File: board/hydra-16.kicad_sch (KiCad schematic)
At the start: 35 parts, among them J1 Conn_01x32, J2 Conn_01x24, J3 DSUB_9, J4 RDY Pull_Up, U1 WDC65C02S, U2 R65C22-P2, U3 R65C51-P2, U4 74F138, U5 MAX232, U6 SST39SF0x0A, U7 HM628512LP-5

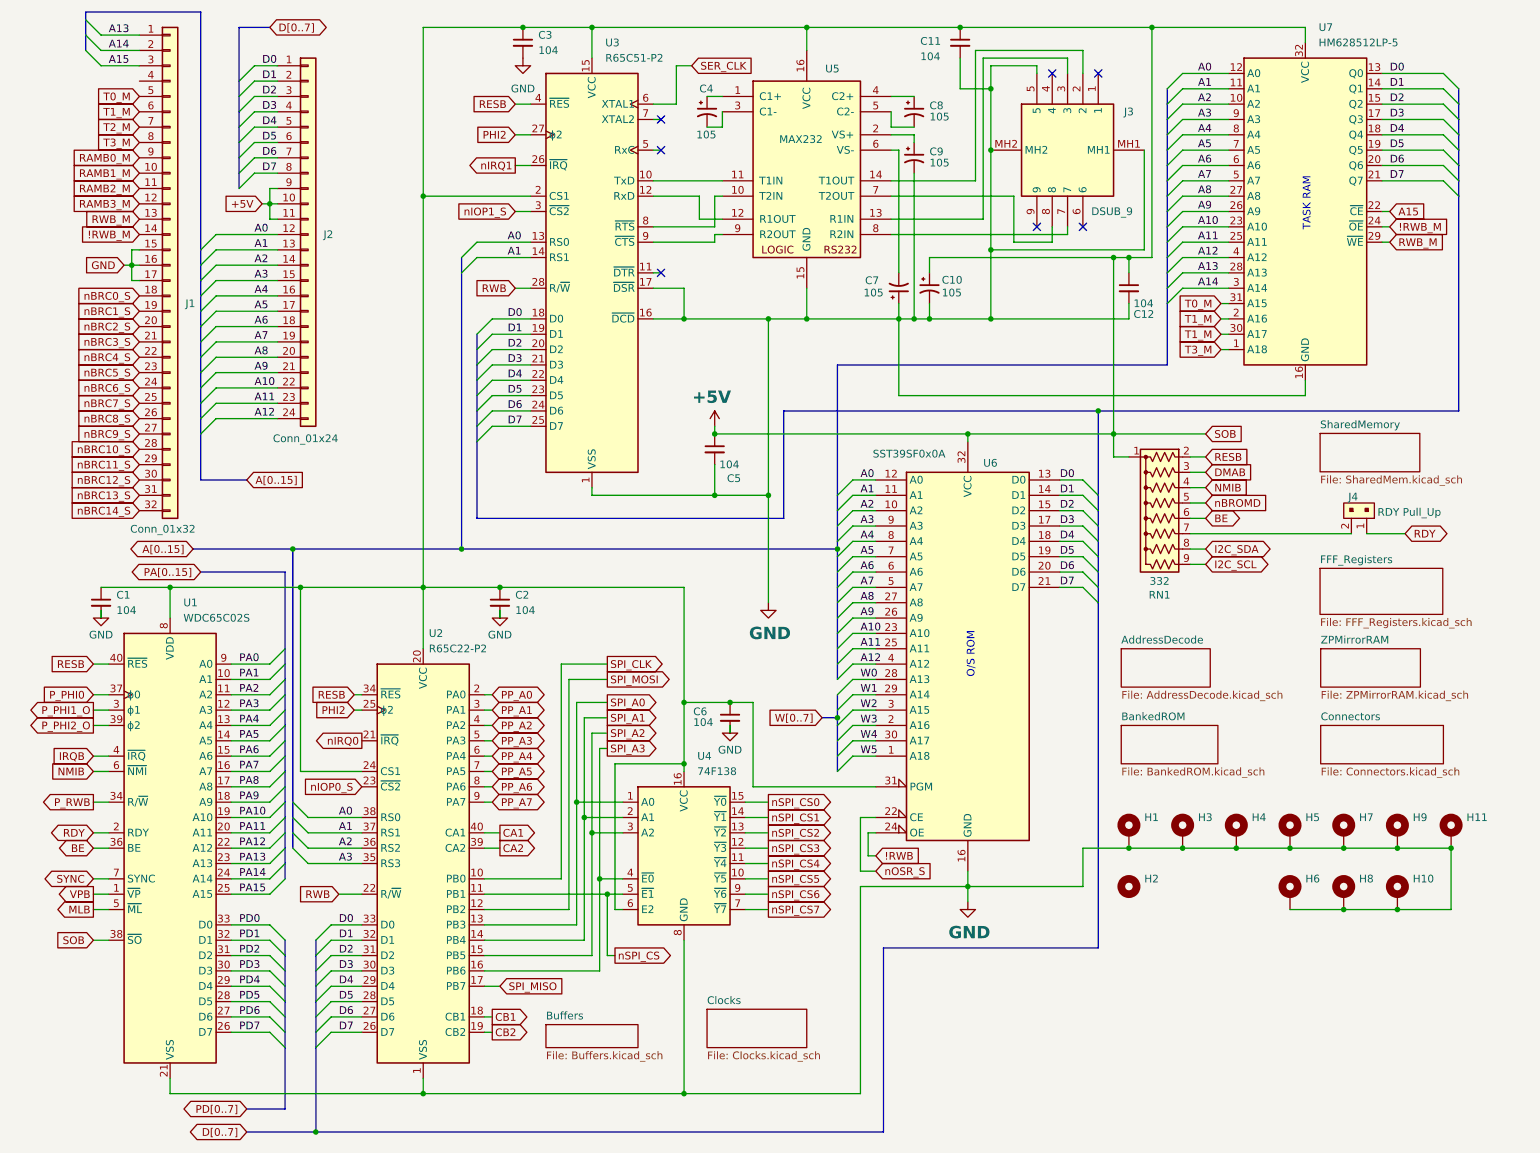
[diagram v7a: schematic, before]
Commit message: 1.7C: Logic corrections and placement tweaks
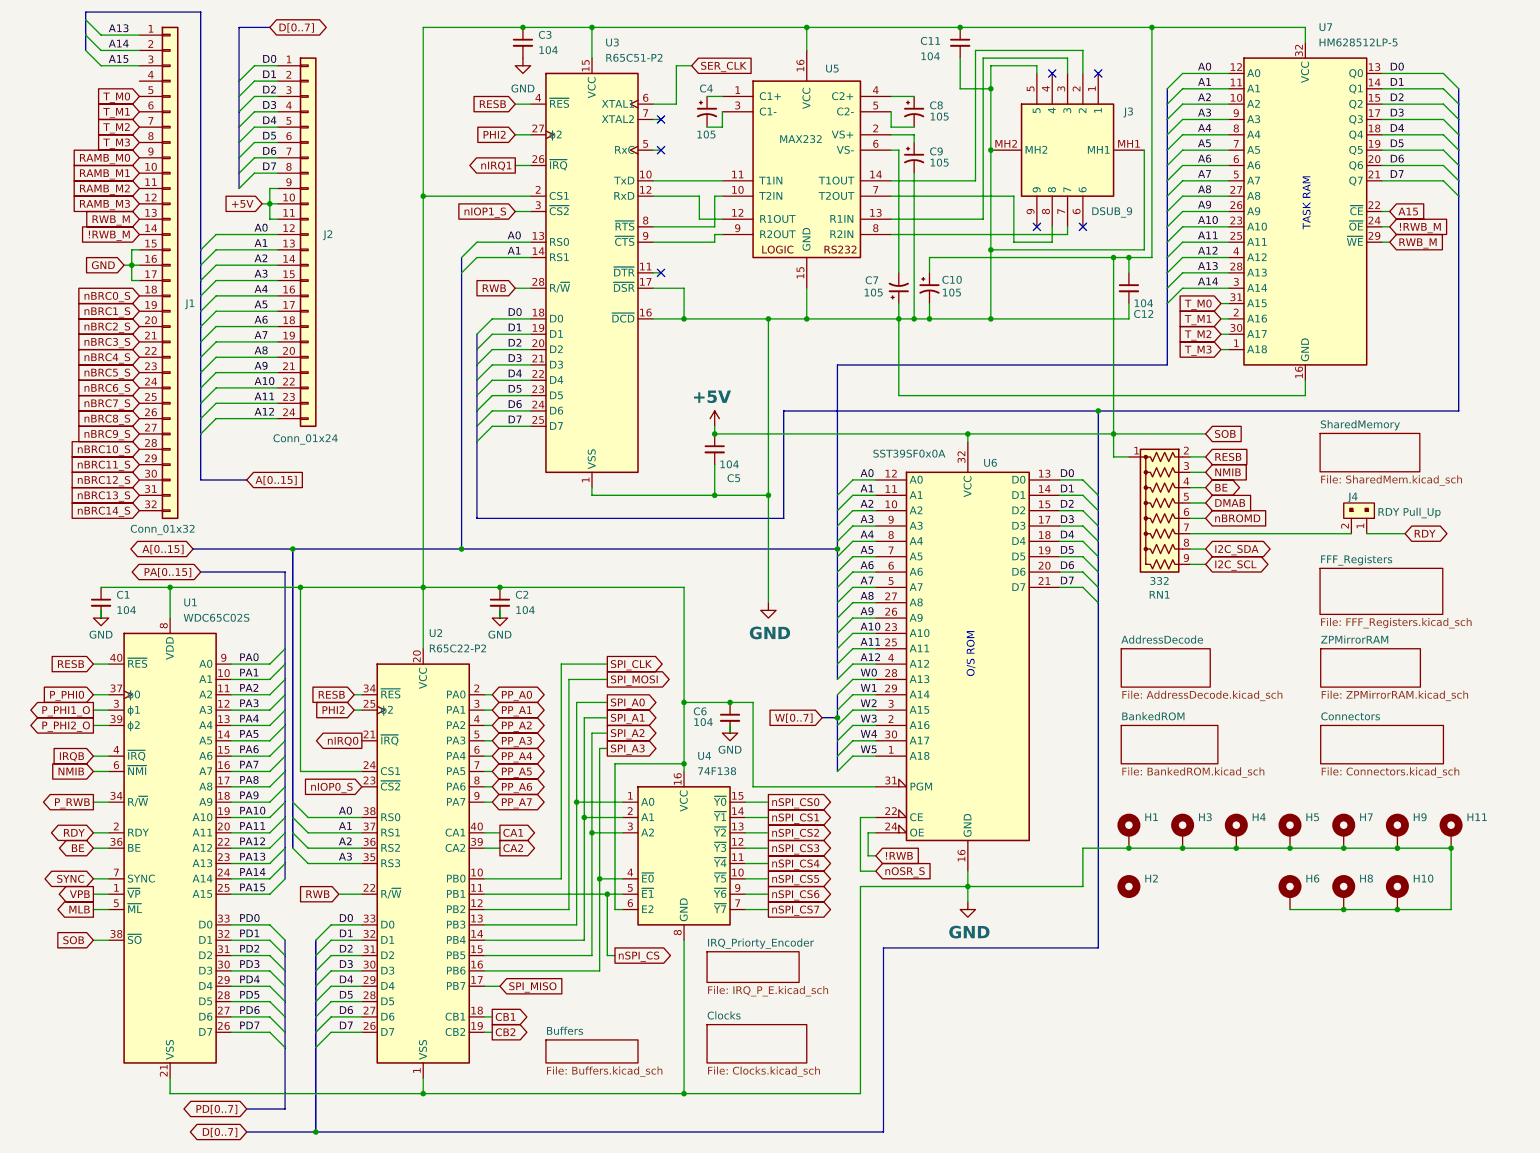
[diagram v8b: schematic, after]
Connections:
- net BE: now also RN1.4 (R3); no longer RN1.6 (R5)
- net DMAB: now also RN1.5 (R4); no longer RN1.3 (R2)
- net NMIB: now also RN1.3 (R2); no longer RN1.4 (R3)
- net nBROMD: now also RN1.6 (R5); no longer RN1.5 (R4)
- net RAMB0_M renamed RAMB_M0
- net RAMB1_M renamed RAMB_M1
- net RAMB2_M renamed RAMB_M2
- net RAMB3_M renamed RAMB_M3
- net T0_M renamed T_M0
- net T1_M renamed T_M1
- net T_M1: no longer U7.30 (A17)
- net T2_M renamed T_M2
- net T_M2: now also U7.30 (A17)
- net T3_M renamed T_M3
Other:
- added sheet IRQ_Priorty_Encoder (IRQ_P_E.kicad_sch)
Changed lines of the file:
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@@
 	(title_block
 		(title "CPU, VIA, ACIA, O/S ROM, Task RAM and Banked RAM Header")
-		(date "2025-09-18")
-		(rev "1.7A")
+		(date "2025-10-01")
+		(rev "1.7C")
 		(company "Data Tuning")
 		(comment 1 "Hydra 16")
@@
 		)
 	)
-	(global_label "T0_M"
+	(global_label "T_M0"
 		(shape input)
 		(at 212.09 62.23 180)
@@
 		)
 	)
-	(global_label "T3_M"
+	(global_label "T_M3"
 		(shape input)
 		(at 212.09 69.85 180)
@@
 		)
 	)
-	(global_label "RAMB1_M"
+	(global_label "nBROMD"
+		(shape input)
+		(at 209.55 97.79 0)
+		(fields_autoplaced yes)
+		(effects
+			(font
+				(size 1.27 1.27)
+			)
+			(justify left)
+		)
+		(property "Intersheetrefs" "${INTERSHEET_REFS}"
+			(at 220.2761 97.79 0)
+			(effects
+				(font
+					(size 1.27 1.27)
+				)
+				(justify left)
+				(hide yes)
+			)
+		)
+	)
+	(global_label "RAMB_M1"
 		(shape input)
 		(at 33.02 40.64 180)
@@
 		)
 	)
-	(global_label "T1_M"
+	(global_label "T_M2"
 		(shape input)
 		(at 212.09 67.31 180)
@@
 		)
 	)
-	(global_label "T2_M"
+	(global_label "T_M2"
 		(shape input)
 		(at 33.02 33.02 180)
@@
 		)
 	)
-	(global_label "T0_M"
+	(global_label "T_M0"
 		(shape input)
 		(at 33.02 27.94 180)
@@
 		)
 	)
-	(global_label "DMAB"
-		(shape input)
-		(at 209.55 90.17 0)
-		(fields_autoplaced yes)
-		(effects
-			(font
-				(size 1.27 1.27)
-			)
-			(justify left)
-		)
-		(property "Intersheetrefs" "${INTERSHEET_REFS}"
-			(at 217.6152 90.17 0)
-			(effects
-				(font
-					(size 1.27 1.27)
-				)
-				(justify left)
-				(hide yes)
-			)
-		)
-	)
 	(global_label "PD[0..7]"
 		(shape tri_state)
@@
 		)
 	)
-	(global_label "RAMB0_M"
+	(global_label "RAMB_M0"
 		(shape input)
 		(at 33.02 38.1 180)
@@
 		)
 	)
-	(global_label "nBROMD"
-		(shape input)
-		(at 209.55 95.25 0)
-		(fields_autoplaced yes)
-		(effects
-			(font
-				(size 1.27 1.27)
-			)
-			(justify left)
-		)
-		(property "Intersheetrefs" "${INTERSHEET_REFS}"
-			(at 220.2761 95.25 0)
-			(effects
-				(font
-					(size 1.27 1.27)
-				)
-				(justify left)
-				(hide yes)
-			)
-		)
-	)
 	(global_label "nBRC3_S"
 		(shape input)
@@
 		)
 	)
-	(global_label "T1_M"
+	(global_label "T_M1"
 		(shape input)
 		(at 212.09 64.77 180)
@@
 		)
 	)
-	(global_label "BE"
-		(shape bidirectional)
-		(at 209.55 97.79 0)
+	(global_label "RESB"
+		(shape input)
+		(at 209.55 87.63 0)
 		(fields_autoplaced yes)
 		(effects
@@
 		)
 		(property "Intersheetrefs" "${INTERSHEET_REFS}"
-			(at 203.0345 97.79 0)
+			(at 201.6663 87.63 0)
 			(effects
 				(font
@@
 		)
 	)
-	(global_label "RESB"
+	(global_label "T_M1"
 		(shape input)
-		(at 209.55 87.63 0)
+		(at 33.02 30.48 180)
 		(fields_autoplaced yes)
 		(effects
@@
 				(size 1.27 1.27)
 			)
-			(justify left)
+			(justify right)
 		)
 		(property "Intersheetrefs" "${INTERSHEET_REFS}"
-			(at 201.6663 87.63 0)
+			(at 25.4387 30.48 0)
 			(effects
 				(font
@@
 		)
 	)
-	(global_label "T1_M"
+	(global_label "!RWB"
 		(shape input)
-		(at 33.02 30.48 180)
+		(at 154.94 153.67 0)
 		(fields_autoplaced yes)
 		(effects
@@
 				(size 1.27 1.27)
 			)
-			(justify right)
+			(justify left)
 		)
 		(property "Intersheetrefs" "${INTERSHEET_REFS}"
-			(at 25.4387 30.48 0)
+			(at 147.3586 153.67 0)
 			(effects
 				(font
@@
 		)
 	)
-	(global_label "!RWB"
-		(shape input)
-		(at 154.94 153.67 0)
+	(global_label "BE"
+		(shape bidirectional)
+		(at 209.55 92.71 0)
 		(fields_autoplaced yes)
 		(effects
@@
 		)
 		(property "Intersheetrefs" "${INTERSHEET_REFS}"
-			(at 147.3586 153.67 0)
+			(at 203.0345 92.71 0)
 			(effects
 				(font
@@
 		)
 	)
-	(global_label "T3_M"
+	(global_label "T_M3"
 		(shape input)
 		(at 33.02 35.56 180)
@@
 		)
 	)
-	(global_label "NMIB"
-		(shape input)
-		(at 209.55 92.71 0)
-		(fields_autoplaced yes)
-		(effects
-			(font
-				(size 1.27 1.27)
-			)
-			(justify left)
-		)
-		(property "Intersheetrefs" "${INTERSHEET_REFS}"
-			(at 201.9081 92.71 0)
-			(effects
-				(font
-					(size 1.27 1.27)
-				)
-				(justify right)
-				(hide yes)
-			)
-		)
-	)
 	(global_label "nBRC11_S"
 		(shape input)
@@
 		)
 	)
-	(global_label "RAMB2_M"
+	(global_label "RAMB_M2"
 		(shape input)
 		(at 33.02 43.18 180)
@@
 		)
 	)
+	(global_label "DMAB"
+		(shape input)
+		(at 209.55 95.25 0)
+		(fields_autoplaced yes)
+		(effects
+			(font
+				(size 1.27 1.27)
+			)
+			(justify left)
+		)
+		(property "Intersheetrefs" "${INTERSHEET_REFS}"
+			(at 217.6152 95.25 0)
+			(effects
+				(font
+					(size 1.27 1.27)
+				)
+				(justify left)
+				(hide yes)
+			)
+		)
+	)
 	(global_label "SOB"
 		(shape input)
@@
 		)
 	)
+	(global_label "NMIB"
+		(shape input)
+		(at 209.55 90.17 0)
+		(fields_autoplaced yes)
+		(effects
+			(font
+				(size 1.27 1.27)
+			)
+			(justify left)
+		)
+		(property "Intersheetrefs" "${INTERSHEET_REFS}"
+			(at 201.9081 90.17 0)
+			(effects
+				(font
+					(size 1.27 1.27)
+				)
+				(justify right)
+				(hide yes)
+			)
+		)
+	)
 	(global_label "IRQB"
 		(shape input)
@@
 		)
 	)
-	(global_label "RAMB3_M"
+	(global_label "RAMB_M3"
 		(shape input)
 		(at 33.02 45.72 180)
@@
 	)
 	(sheet
-		(at 127 179.07)
+		(at 127 181.61)
 		(size 16.51 6.35)
 		(exclude_from_sim no)
@@
 		)
 		(property "Sheetname" "Clocks"
-			(at 127 178.3584 0)
+			(at 127 180.8984 0)
 			(effects
 				(font
@@
 		)
 		(property "Sheetfile" "Clocks.kicad_sch"
-			(at 127 186.0046 0)
+			(at 127 188.5446 0)
 			(effects
 				(font
@@
 	)
 	(sheet
-		(at 100.33 181.61)
+		(at 100.33 184.15)
 		(size 15.24 3.81)
 		(exclude_from_sim no)
@@
 		)
 		(property "Sheetname" "Buffers"
-			(at 100.33 180.8984 0)
+			(at 100.33 183.4384 0)
 			(effects
 				(font
@@
 		)
 		(property "Sheetfile" "Buffers.kicad_sch"
-			(at 100.33 186.0046 0)
+			(at 100.33 188.5446 0)
 			(effects
 				(font
@@
 				)
 			)
+		)
+	)
+	(sheet
+		(at 127 169.545)
+		(size 15.24 5.08)
+		(exclude_from_sim no)
+		(in_bom yes)
+		(on_board yes)
+		(dnp no)
+		(fields_autoplaced yes)
+		(stroke
+			(width 0.1524)
+			(type solid)
+		)
+		(fill
+			(color 0 0 0 0.0000)
+		)
+		(property "Sheetname" "IRQ_Priorty_Encoder"
+			(at 127 168.8334 0)
+			(effects
+				(font
+					(size 1.27 1.27)
+				)
+				(justify left bottom)
+			)
+		)
+		(property "Sheetfile" "IRQ_P_E.kicad_sch"
+			(at 127 175.2096 0)
+			(effects
+				(font
+					(size 1.27 1.27)
+				)
+				(justify left top)
+			)
+		)
+		(instances
+			(project "hydra-16"
+				(path "/ef29fc71-3fec-48b5-8a1a-46bee537a98c"
+					(page "8")
+				)
+			)
